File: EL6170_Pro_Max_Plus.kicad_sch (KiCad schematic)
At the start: 101 parts, among them CN1 PJ-327A0-SMT, J1 USB_C_Receptacle, J2 microSD, Q1 MMBT3904, Q2 MMBT3904, Q3 2N7002, Q4 AO3401A, Q5 AO3401A, SW1 RST, SW2 BOOT, U1 ESP32-S3, U10 ME6211C33M5, U11 TP5400_C2891434, U2 TPS61040DBV, U3 ESP-PSRAM64H, U4 W25Q128JVS, U5 ME6217C33M5, U6 CH340K, U7 RFANT5220110A0T, U8 CH334R, U9 PCM5102A, X1 40MHz, X2 12MHz

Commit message: sync
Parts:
- added SW1: SW_Push, symbol Switch:SW_Push
- renumbered SW2 to SWBOOT, SW1 to SWRST
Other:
- moved on the sheet: C36, C37, C38, C39, C40, C41, C42, C43, D1, D4, D5, L6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

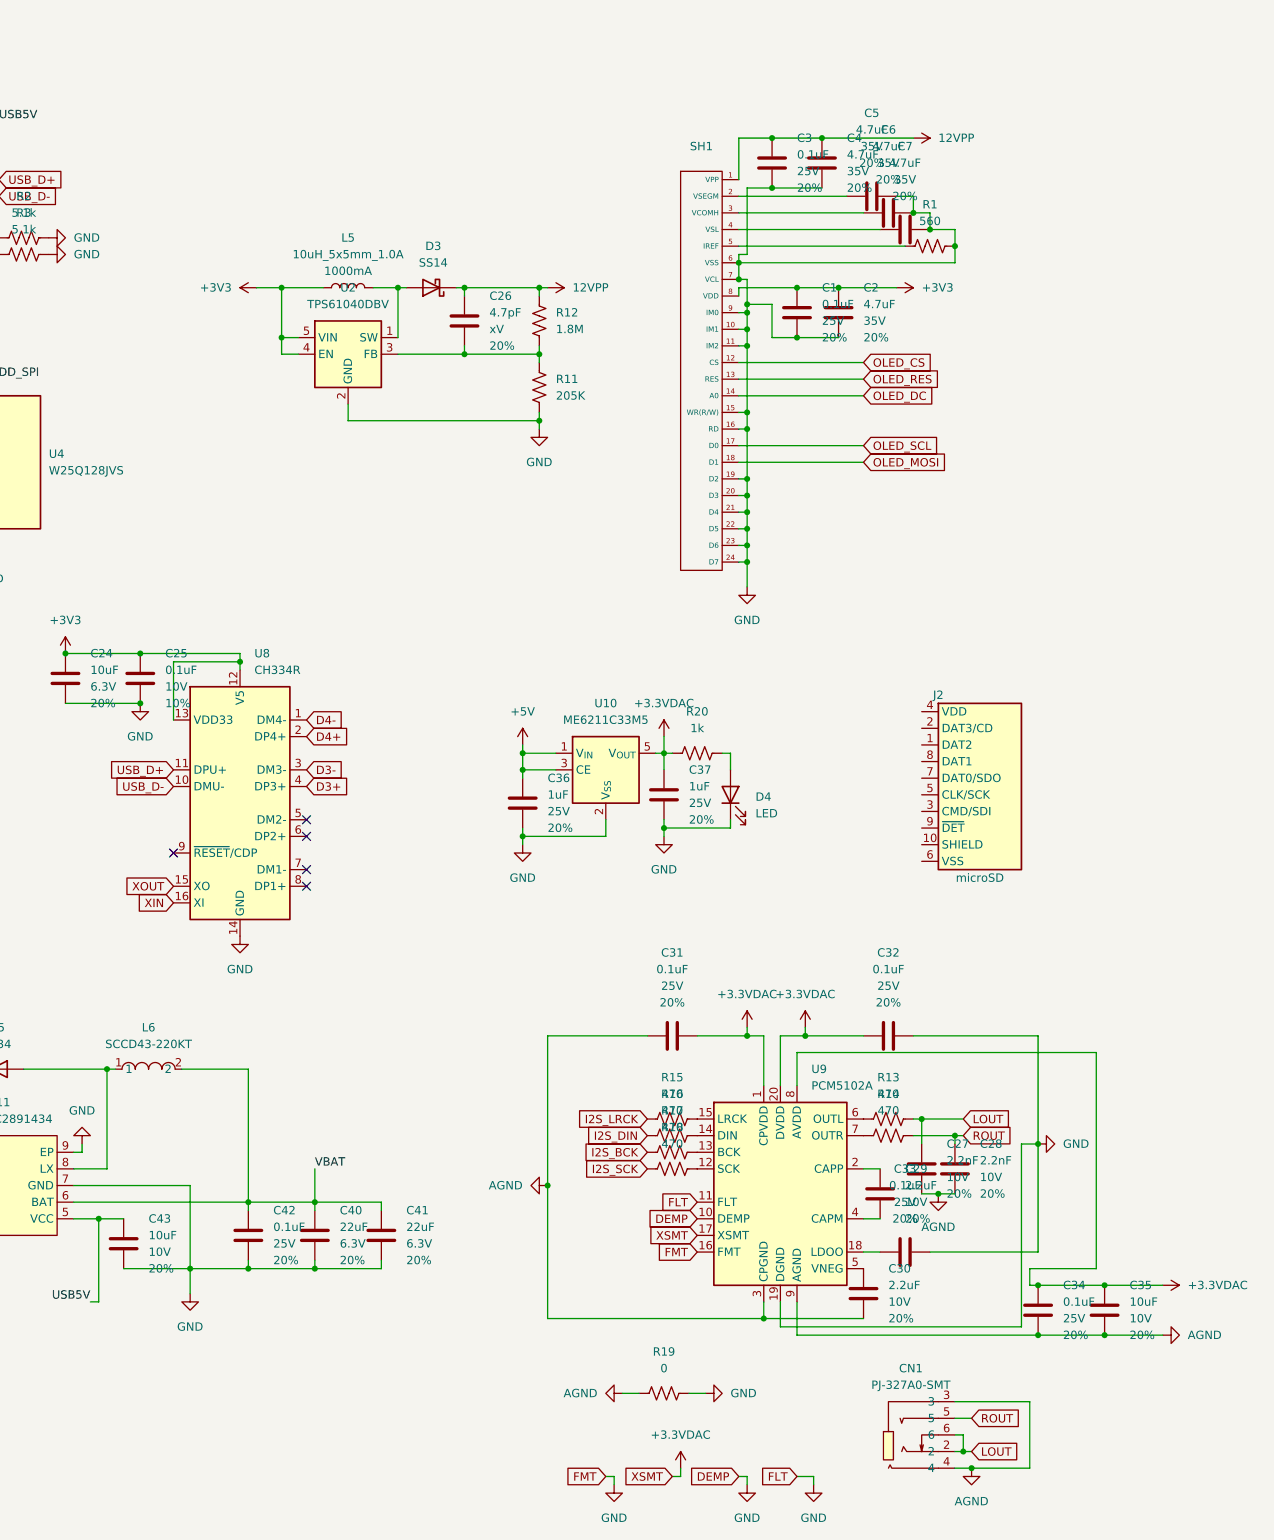
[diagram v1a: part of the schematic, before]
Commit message: add SDCARD
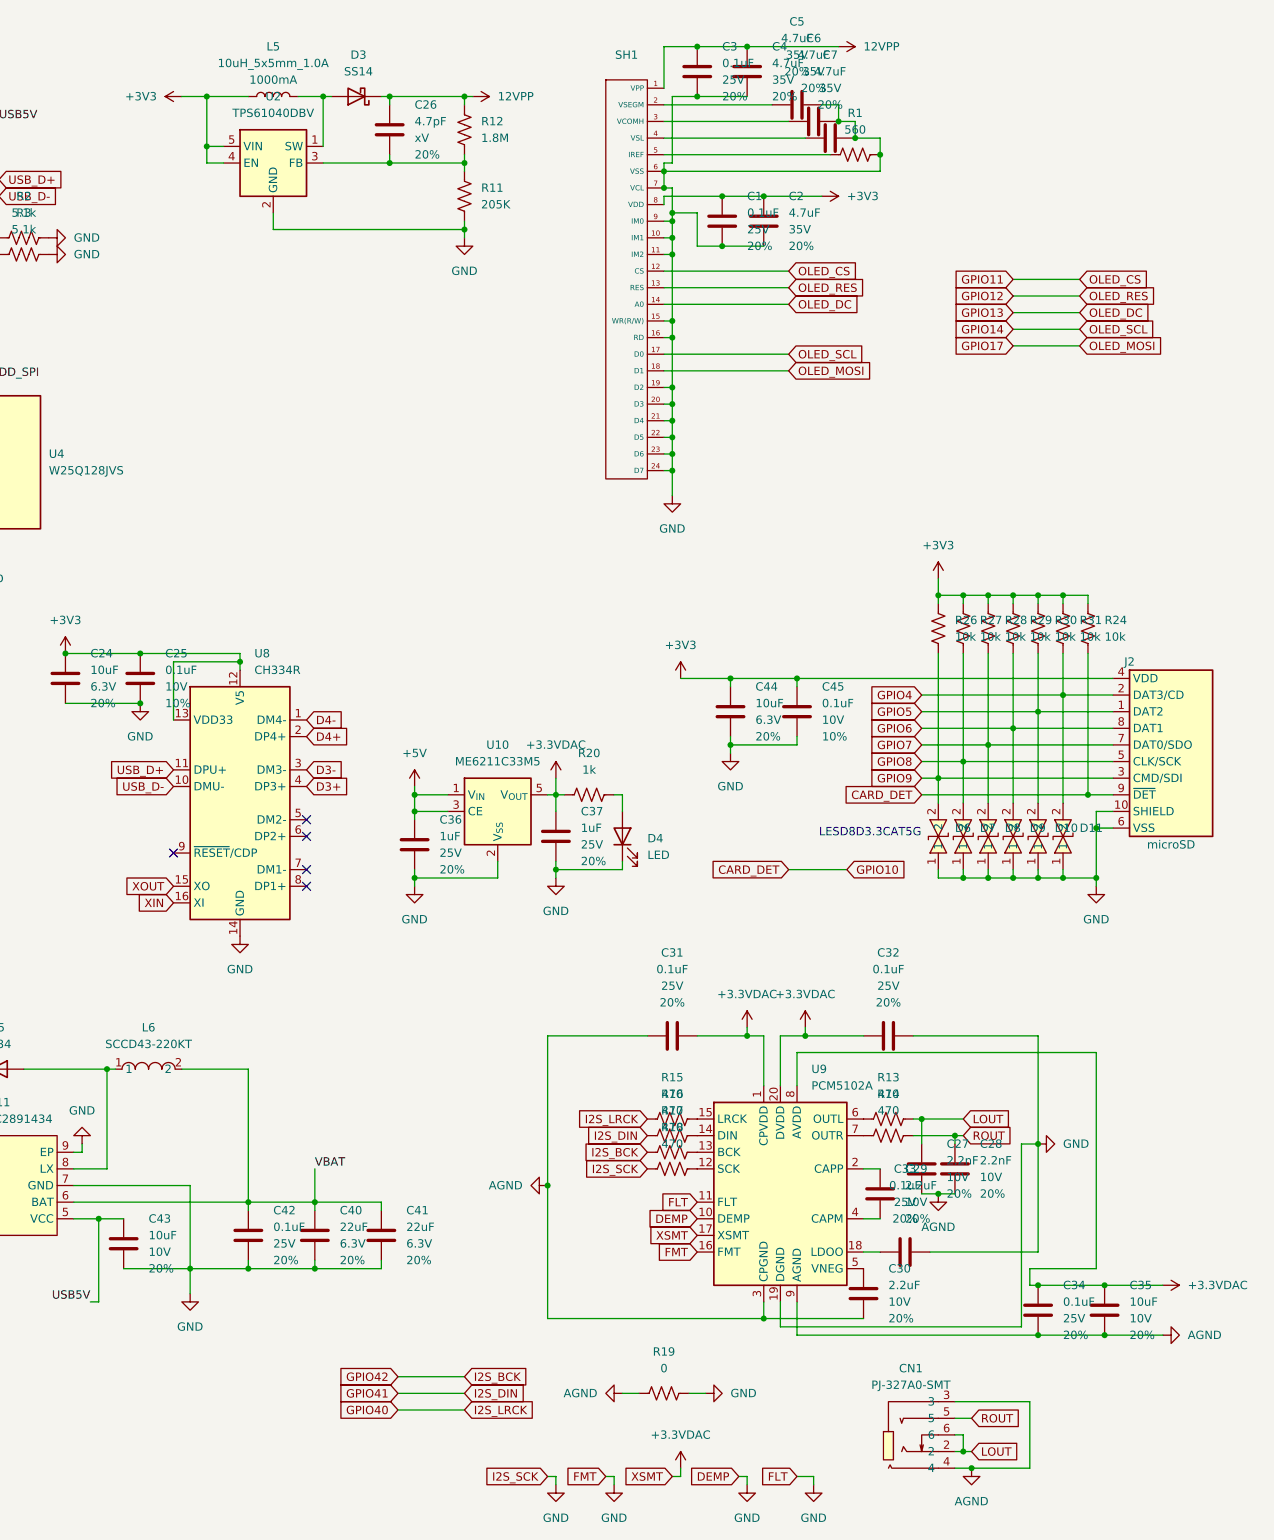
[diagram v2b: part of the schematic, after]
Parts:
- added C44: 10uF, SparkFun-Capacitor:C_0402_1005Metric, symbol SparkFun-Capacitor:10uF_0402_6.3V_20%
- added C45: 0.1uF, SparkFun-Capacitor:C_0402_1005Metric, symbol SparkFun-Capacitor:0.1uF_0402_10V_10%
- added D10, D11, D6, D7, D8, D9: LESD8D3.3CAT5G, Diode_SMD:D_SOD-882, symbol easyeda2kicad:LESD8D3.3CAT5G
- added R24, R26, R27, R28, R29, R30, R31: 10k, SparkFun-Resistor:R_0402_1005Metric, symbol SparkFun-Resistor:10k_0402
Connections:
- net GPIO10 is gone; now on net CARD_DET: U1.15 (GPIO10)
- net I2S_BCK is gone; now on net GPIO42: R17.2
- net I2S_DIN is gone; now on net GPIO41: R16.2
- net I2S_LRCK is gone; now on net GPIO40: R15.2
- net I2S_SCK is gone; now on net GND: R18.2
- net OLED_CS is gone; now on net GPIO11: SH1.12 (CS)
- net OLED_DC is gone; now on net GPIO13: SH1.14 (A0)
- net OLED_MOSI is gone; now on net GPIO17: SH1.18 (D1)
- net OLED_RES is gone; now on net GPIO12: SH1.13 (RES)
- net OLED_SCL is gone; now on net GPIO14: SH1.17 (D0)
- net +3V3: now also J2.4 (VDD), C44.1, C45.1, R24.1, R26.1, R27.1, R28.1, R29.1, R30.1, R31.1
- net GND: now also J2.10 (SHIELD), J2.6 (VSS), C44.2, C45.2, D10.1, D11.1, D6.1, D7.1, D8.1, D9.1
- net GPIO4: now also J2.2 (DAT3/CD), D11.2, R31.2
- net GPIO5: now also J2.1 (DAT2), D10.2, R30.2
- net GPIO6: now also J2.8 (DAT1), D9.2, R29.2
- net GPIO7: now also J2.7 (DAT0/SDO), D8.2, R28.2
- net GPIO8: now also J2.5 (CLK/SCK), D7.2, R27.2
- net GPIO9: now also J2.3 (CMD/SDI), D6.2, R26.2
- net CARD_DET: now reaches J2.9 (~{DET})
- net CARD_DET: now also R24.2
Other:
- note added: "LESD8D3.3CAT5G"
- moved on the sheet: C1, C2, C26, C3, C36, C37, C4, C5, C6, C7, D3, D4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

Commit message: sync
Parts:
- added R25, R32, R33: 10k, SparkFun-Resistor:R_0402_1005Metric, symbol SparkFun-Resistor:10k_0402
- added U12: PCF8575DBR, Package_SO:SSOP-24_5.3x8.2mm_P0.65mm, symbol Interface_Expansion:PCF8575DBR
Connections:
- net +3V3: now also R25.1, R32.1, R33.1
- net GND: now also U12.12 (GND), U12.2 (A1), U12.21 (A0), U12.3 (A2)
- net GPIO21: now also R33.2, U12.1 (~{INT})
- net GPIO38: now also R25.2, U12.22 (SCL)
- net GPIO39: now also R32.2, U12.23 (SDA)

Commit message: 原理图搞定啦啊哈哈哈！！！
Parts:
- added D12, D13, D14, D15, D16, D17, D18, D19, D20, D21, D22, D23, D24, D25, D26, D27, D28, D29, D30, D31, D32, D33, D34, D35, D36, D37, D38, D39, D40, D41, D42, D43, D44, D45, D46, D47, D48, D49, D50, D51, D52, D53, D54, D55, D56, D57, D58, D59, D60, D61, D62, D63, D64: 1N4148WS, Diode_SMD:D_SOD-323, symbol Diode:1N4148WS
- added SW10: SW_K4, Butm:MaskBtm4mmBh, symbol Switch:SW_Push
- added SW11: SW_K5, Butm:MaskBtm4mmBh, symbol Switch:SW_Push
- added SW12: SW_K6, Butm:MaskBtm4mmBh, symbol Switch:SW_Push
- added SW13: SW_K7, Butm:MaskBtm4mmBh, symbol Switch:SW_Push
- added SW14: SW_K8, Butm:MaskBtm4mmBh, symbol Switch:SW_Push
- added SW15: SW_K9, Butm:MaskBtm4mmBh, symbol Switch:SW_Push
- added SW16: SW_K0, Butm:MaskBtm4mmBh, symbol Switch:SW_Push
- added SW17: SW_KQ, Butm:MaskBtm5mm, symbol Switch:SW_Push
- added SW18: SW_KW, Butm:MaskBtm5mm, symbol Switch:SW_Push
- added SW19: SW_KE, Butm:MaskBtm5mm, symbol Switch:SW_Push
- added SW2: SW_UP, Butm:MaskBtm6mm, symbol Switch:SW_Push
- added SW20: SW_KR, Butm:MaskBtm5mm, symbol Switch:SW_Push
- added SW21: SW_KT, Butm:MaskBtm5mm, symbol Switch:SW_Push
- added SW22: SW_KY, Butm:MaskBtm5mm, symbol Switch:SW_Push
- added SW23: SW_KU, Butm:MaskBtm5mm, symbol Switch:SW_Push
- added SW24: SW_KI, Butm:MaskBtm5mm, symbol Switch:SW_Push
- added SW25: SW_KO, Butm:MaskBtm5mm, symbol Switch:SW_Push
- added SW26: SW_KP, Butm:MaskBtm5mm, symbol Switch:SW_Push
- added SW27: SW_KA, Butm:MaskBtm5mm, symbol Switch:SW_Push
- added SW28: SW_KS, Butm:MaskBtm5mm, symbol Switch:SW_Push
- added SW29: SW_KD, Butm:MaskBtm5mm, symbol Switch:SW_Push
- added SW3: SW_DOWN, Butm:MaskBtm6mm, symbol Switch:SW_Push
- added SW30: SW_KF, Butm:MaskBtm5mm, symbol Switch:SW_Push
- added SW31: SW_KG, Butm:MaskBtm5mm, symbol Switch:SW_Push
- added SW32: SW_KH, Butm:MaskBtm5mm, symbol Switch:SW_Push
- added SW33: SW_KJ, Butm:MaskBtm5mm, symbol Switch:SW_Push
- added SW34: SW_KK, Butm:MaskBtm5mm, symbol Switch:SW_Push
- added SW35: SW_KL, Butm:MaskBtm5mm, symbol Switch:SW_Push
- added SW36: SW_KZ, Butm:MaskBtm5mm, symbol Switch:SW_Push
- added SW37: SW_KX, Butm:MaskBtm5mm, symbol Switch:SW_Push
- added SW38: SW_KC, Butm:MaskBtm5mm, symbol Switch:SW_Push
- added SW39: SW_KV, Butm:MaskBtm5mm, symbol Switch:SW_Push
- added SW4: SW_RIGHT, Butm:MaskBtm6mmBh, symbol Switch:SW_Push
- added SW40: SW_KB, Butm:MaskBtm5mm, symbol Switch:SW_Push
- added SW41: SW_KN, Butm:MaskBtm5mm, symbol Switch:SW_Push
- added SW42: SW_KM, Butm:MaskBtm5mm, symbol Switch:SW_Push
- added SW43: SW_KCOM, Butm:MaskBtm5mm, symbol Switch:SW_Push
- added SW44: SW_KDOT, Butm:MaskBtm5mm, symbol Switch:SW_Push
- added SW45: SW_SHIFT, Butm:MaskBtm5mm, symbol Switch:SW_Push
- added SW46: SW_CE(IO0), Butm:MaskBtm5mm, symbol Switch:SW_Push
- added SW47: SW_OFF, Butm:MaskBtm5mm, symbol Switch:SW_Push
- added SW48: SW_SECRET, Butm:MaskBtm5mm, symbol Switch:SW_Push
- added SW49: SW_MCK, Butm:MaskBtm5mm, symbol Switch:SW_Push
- added SW5: SW_UP2, Butm:MaskBtm6mm, symbol Switch:SW_Push
- added SW50: SW_SPACE, Butm:MaskBtm5mmBh, symbol Switch:SW_Push
- added SW51: SW_REMARK, Butm:MaskBtm5mm, symbol Switch:SW_Push
- added SW52: SW_CALENDAR, Butm:MaskBtm5mm, symbol Switch:SW_Push
- added SW53: SW_MODE, Butm:MaskBtm5mm, symbol Switch:SW_Push
- added SW54: SW_ENTER, Butm:MaskBtm5mmBh, symbol Switch:SW_Push
- added SW6: SW_DOWN2, Butm:MaskBtm6mm, symbol Switch:SW_Push
- added SW7: SW_K1, Butm:MaskBtm4mmBh, symbol Switch:SW_Push
- added SW8: SW_K2, Butm:MaskBtm4mmBh, symbol Switch:SW_Push
- added SW9: SW_K3, Butm:MaskBtm4mmBh, symbol Switch:SW_Push
- SW1: value SW_Push -> SW_LEFT; footprint (none) -> Butm:MaskBtm6mmBh
- SWBOOT1: renamed from SWBOOT; footprint (none) -> Butm:MaskBtm4mm
- SWRST1: renamed from SWRST; footprint (none) -> Butm:MaskBtm4mm
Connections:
- net GND: now also SW46.1
- net GPIO0: now also SW46.2
- net KEY_COL0: now reaches SW1.1
- net KEY_COL0: now also U12.4 (P0), SW17.1, SW25.1, SW33.1, SW41.1, SW50.1, SW9.1
- net at SW1.2: now also D12.2 (A)
- net KEY_COL6: now reaches U12.10 (P6)
- net KEY_COL6: now also SW15.1, SW23.1, SW31.1, SW39.1, SW48.1, SW7.1
- net KEY_COL7: now reaches U12.11 (P7)
- net KEY_COL7: now also SW16.1, SW24.1, SW32.1, SW40.1, SW49.1, SW8.1
- net KEY_ROW0: now reaches U12.13 (P10)
- net KEY_ROW0: now also D12.1 (K), D13.1 (K), D14.1 (K), D15.1 (K), D16.1 (K), D17.1 (K), D18.1 (K), D19.1 (K)
- net KEY_ROW1: now reaches U12.14 (P11)
- net KEY_ROW1: now also D20.1 (K), D21.1 (K), D22.1 (K), D23.1 (K), D24.1 (K), D25.1 (K), D26.1 (K), D27.1 (K)
- net KEY_ROW2: now reaches U12.15 (P12)
- net KEY_ROW2: now also D28.1 (K), D29.1 (K), D30.1 (K), D31.1 (K), D32.1 (K), D33.1 (K), D34.1 (K), D35.1 (K)
- net KEY_ROW3: now reaches U12.16 (P13)
- net KEY_ROW3: now also D36.1 (K), D37.1 (K), D38.1 (K), D39.1 (K), D40.1 (K), D41.1 (K), D42.1 (K), D43.1 (K)
- net KEY_ROW4: now reaches U12.17 (P14)
- net KEY_ROW4: now also D44.1 (K), D45.1 (K), D46.1 (K), D47.1 (K), D48.1 (K), D49.1 (K), D50.1 (K), D51.1 (K)
- net KEY_ROW5: now reaches U12.18 (P15)
- net KEY_ROW5: now also D52.1 (K), D53.1 (K), D54.1 (K), D55.1 (K), D56.1 (K), D57.1 (K), D58.1 (K), D59.1 (K)
- net KEY_ROW6: now reaches U12.19 (P16)
- net KEY_ROW6: now also D60.1 (K), D61.1 (K), D62.1 (K), D63.1 (K), D64.1 (K)
- net KEY_COL1: now reaches U12.5 (P1)
- net KEY_COL1: now also SW10.1, SW18.1, SW2.1, SW26.1, SW34.1, SW42.1, SW51.1
- net KEY_COL2: now reaches U12.6 (P2)
- net KEY_COL2: now also SW11.1, SW19.1, SW27.1, SW3.1, SW35.1, SW43.1, SW52.1
- net KEY_COL3: now reaches U12.7 (P3)
- net KEY_COL3: now also SW12.1, SW20.1, SW28.1, SW36.1, SW4.1, SW44.1, SW53.1
- net KEY_COL4: now reaches U12.8 (P4)
- net KEY_COL4: now also SW13.1, SW21.1, SW29.1, SW37.1, SW45.1, SW5.1, SW54.1
- net KEY_COL5: now reaches U12.9 (P5)
- net KEY_COL5: now also SW14.1, SW22.1, SW30.1, SW38.1, SW47.1, SW6.1
- new net: D59.2 (A), SW41.2
- new net: D25.2 (A), SW14.2
- new net: D37.2 (A), SW26.2
- new net: D62.2 (A), SW52.2
- new net: D18.2 (A), SW7.2
- new net: D51.2 (A), SW40.2
- new net: D39.2 (A), SW28.2
- new net: D48.2 (A), SW37.2
- new net: D19.2 (A), SW8.2
- new net: D57.2 (A), SW43.2
- new net: D26.2 (A), SW15.2
- new net: D60.2 (A), SW50.2
- new net: D31.2 (A), SW20.2
- new net: D49.2 (A), SW38.2
- new net: D54.2 (A), SW47.2
- new net: D32.2 (A), SW21.2
- new net: D29.2 (A), SW18.2
- new net: D47.2 (A), SW36.2
- new net: D16.2 (A), SW5.2
- new net: D27.2 (A), SW16.2
- new net: D35.2 (A), SW24.2
- new net: D13.2 (A), SW2.2
- new net: D45.2 (A), SW34.2
- new net: D41.2 (A), SW30.2
- new net: D24.2 (A), SW13.2
- new net: D28.2 (A), SW17.2
- new net: D46.2 (A), SW35.2
- new net: D22.2 (A), SW11.2
- new net: D42.2 (A), SW31.2
- new net: D56.2 (A), SW44.2
- new net: D14.2 (A), SW3.2
- new net: D17.2 (A), SW6.2
- new net: D55.2 (A), SW45.2
- new net: D64.2 (A), SW54.2
- new net: D50.2 (A), SW39.2
- new net: D52.2 (A), SW49.2
- new net: D30.2 (A), SW19.2
- new net: D23.2 (A), SW12.2
- new net: D61.2 (A), SW51.2
- new net: D21.2 (A), SW10.2
- new net: D15.2 (A), SW4.2
- new net: D44.2 (A), SW33.2
- new net: D20.2 (A), SW9.2
- new net: D38.2 (A), SW27.2
- new net: D33.2 (A), SW22.2
- new net: D40.2 (A), SW29.2
- new net: D36.2 (A), SW25.2
- new net: D63.2 (A), SW53.2
- new net: D43.2 (A), SW32.2
- new net: D34.2 (A), SW23.2
- new net: D53.2 (A), SW48.2
- new net: D58.2 (A), SW42.2
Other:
- moved on the sheet: C38, C39, C40, C41, C42, C43, D5, L6, Q3, Q4, Q5, R21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

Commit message: key
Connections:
- net +3V3: now also U12.24 (VCC)
- no-connect marks 7 -> 8
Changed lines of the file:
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@@
 	)
 	(no_connect
+		(at 78.74 261.62)
+	)
+	(no_connect
 		(at 261.62 137.16)
 	)
@@
 					(unit 1)
 				)
+			)
+		)
+	)
+	(symbol
+		(lib_id "power:+3V3")
+		(at 68.58 215.9 0)
+		(unit 1)
+		(exclude_from_sim no)
+		(in_bom yes)
+		(on_board yes)
+		(dnp no)
+		(fields_autoplaced yes)
+		(property "Reference" "#PWR087"
+			(at 68.58 219.71 0)
+			(effects
+				(font
+					(size 1.27 1.27)
+				)
+				(hide yes)
+			)
+		)
+		(property "Value" "+3V3"
+			(at 68.58 210.82 0)
+			(effects
+				(font
+					(size 1.27 1.27)
+				)
+			)
+		)
+		(property "Footprint" ""
+			(at 68.58 215.9 0)
+			(effects
+				(font
+					(size 1.27 1.27)
+				)
+				(hide yes)
+			)
+		)
+		(property "Datasheet" ""
+			(at 68.58 215.9 0)
+			(effects
+				(font
+					(size 1.27 1.27)
+				)
+				(hide yes)
+			)
+		)
+		(property "Description" "Power symbol creates a global label with name \"+3V3\""
+			(at 68.58 215.9 0)
+			(effects
+				(font
+					(size 1.27 1.27)
+				)
+				(hide yes)
+			)
+		)
+		(pin "1"
+		)
+		(instances
+			(project "EL6170_Pro_Max_Plus"
+				(path "/b3287cc9-c0c8-4939-96d8-31efd376f189"
+					(reference "#PWR087")
+					(unit 1)
+				)

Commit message: sync
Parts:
- added BAT+, BAT-: ~, TestPoint:TestPoint_Pad_2.0x2.0mm, symbol PAD:PAD
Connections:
- net GND: now also BAT-.1
- net VBAT: now also BAT+.1
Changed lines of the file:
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@@
 	(wire
 		(pts
+			(xy 262.89 77.47) (xy 262.89 76.2)
+		)
+		(stroke
+			(width 0)
+			(type default)
+		)
+	)
+	(wire
+		(pts
 			(xy 316.23 60.96) (xy 317.5 60.96)
 		)
@@
 	(wire
 		(pts
+			(xy 252.73 78.74) (xy 251.46 78.74)
+		)
+		(stroke
+			(width 0)
+			(type default)
+		)
+	)
+	(wire
+		(pts
 			(xy 180.34 264.16) (xy 180.34 279.4)
 		)
@@
 	(wire
 		(pts
+			(xy 251.46 78.74) (xy 251.46 76.2)
+		)
+		(stroke
+			(width 0)
+			(type default)
+		)
+	)
+	(wire
+		(pts
 			(xy 336.55 177.8) (xy 336.55 172.72)
 		)
@@
 		)
 	)
+	(label "VBAT"
+		(at 252.73 78.74 0)
+		(fields_autoplaced yes)
+		(effects
+			(font
+				(size 1.27 1.27)
+			)
+			(justify left bottom)
+		)
+	)
 	(global_label "GPIO35"
 		(shape input)
@@
 	)
 	(symbol
+		(lib_id "power:GND")
+		(at 262.89 77.47 0)
+		(unit 1)
+		(exclude_from_sim no)
+		(in_bom yes)
+		(on_board yes)
+		(dnp no)
+		(fields_autoplaced yes)
+		(property "Reference" "#PWR088"
+			(at 262.89 83.82 0)
+			(effects
+				(font
+					(size 1.27 1.27)
+				)
+				(hide yes)
+			)
+		)
+		(property "Value" "GND"
+			(at 262.89 82.55 0)
+			(effects
+				(font
+					(size 1.27 1.27)
+				)
+			)
+		)
+		(property "Footprint" ""
+			(at 262.89 77.47 0)
+			(effects
+				(font
+					(size 1.27 1.27)
+				)
+				(hide yes)
+			)
+		)
+		(property "Datasheet" ""
+			(at 262.89 77.47 0)
+			(effects
+				(font
+					(size 1.27 1.27)
+				)
+				(hide yes)
+			)
+		)
+		(property "Description" "Power symbol creates a global label with name \"GND\" , ground"
+			(at 262.89 77.47 0)
+			(effects
+				(font
+					(size 1.27 1.27)
+				)
+				(hide yes)
+			)
+		)
+		(pin "1"
+		)
+		(instances
+			(project "EL6170_Pro_Max_Plus"
+				(path "/b3287cc9-c0c8-4939-96d8-31efd376f189"
+					(reference "#PWR088")
+					(unit 1)
+				)
+			)
+		)
+	)
+	(symbol
 		(lib_id "SparkFun-Resistor:330_0603")
 		(at 152.4 185.42 90)
@@
 	)
 	(symbol
+		(lib_id "PAD:PAD")
+		(at 251.46 73.66 0)
+		(unit 1)
+		(exclude_from_sim no)
+		(in_bom yes)
+		(on_board yes)
+		(dnp no)
+		(fields_autoplaced yes)
+		(property "Reference" "BAT+"
+			(at 254 71.7549 0)
+			(effects
+				(font
+					(size 1.27 1.27)
+				)
+				(justify left)
+			)
+		)
+		(property "Value" "~"
+			(at 254 73.66 0)
+			(effects
+				(font
+					(size 1.27 1.27)
+				)
+				(justify left)
+			)
+		)
+		(property "Footprint" "TestPoint:TestPoint_Pad_2.0x2.0mm"
+			(at 251.46 73.66 0)
+			(effects
+				(font
+					(size 1.27 1.27)
+				)
+				(hide yes)
+			)
+		)
+		(property "Datasheet" ""
+			(at 251.46 73.66 0)
+			(effects
+				(font
+					(size 1.27 1.27)
+				)
+				(hide yes)
+			)
+		)
+		(property "Description" ""
+			(at 251.46 73.66 0)
+			(effects
+				(font
+					(size 1.27 1.27)
+				)
+				(hide yes)
+			)
+		)
+		(pin "1"
+		)
+		(instances
+			(project ""
+				(path "/b3287cc9-c0c8-4939-96d8-31efd376f189"
+					(reference "BAT+")
+					(unit 1)
+				)
+			)
+		)
+	)
+	(symbol
 		(lib_name "GND_1")
 		(lib_id "power:GND")
@@
 					(unit 1)
 				)
+			)
+		)
+	)
+	(symbol
+		(lib_id "PAD:PAD")
+		(at 262.89 73.66 0)
+		(unit 1)
+		(exclude_from_sim no)
+		(in_bom yes)
+		(on_board yes)
+		(dnp no)
+		(fields_autoplaced yes)
+		(property "Reference" "BAT-"
+			(at 265.43 71.7549 0)
+			(effects
+				(font
+					(size 1.27 1.27)
+				)
+				(justify left)
+			)
+		)
+		(property "Value" "~"
+			(at 265.43 73.66 0)
+			(effects
+				(font
+					(size 1.27 1.27)
+				)
+				(justify left)
+			)
+		)
+		(property "Footprint" "TestPoint:TestPoint_Pad_2.0x2.0mm"
+			(at 262.89 73.66 0)
+			(effects
+				(font
+					(size 1.27 1.27)
+				)
+				(hide yes)
+			)
+		)
+		(property "Datasheet" ""
+			(at 262.89 73.66 0)
+			(effects
+				(font
+					(size 1.27 1.27)
+				)
+				(hide yes)
+			)
+		)
+		(property "Description" ""
+			(at 262.89 73.66 0)
+			(effects
+				(font
+					(size 1.27 1.27)
+				)
+				(hide yes)
+			)
+		)
+		(pin "1"
+		)
+		(instances
+			(project "EL6170_Pro_Max_Plus"
+				(path "/b3287cc9-c0c8-4939-96d8-31efd376f189"
+					(reference "BAT-")
+					(unit 1)
+				)
